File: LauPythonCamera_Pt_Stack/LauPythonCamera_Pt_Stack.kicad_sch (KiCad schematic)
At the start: 42 parts, among them J1 DF40C-80DP (Bank A), J2 DF40C-80DP (Bank B), J3 DF40C-50DP (Control), U1 NOIP1SN1300A-QDI, U2 AP2112K-1.8 LDO, U3 Load switch 3V3, U4 ADP7158-3.3

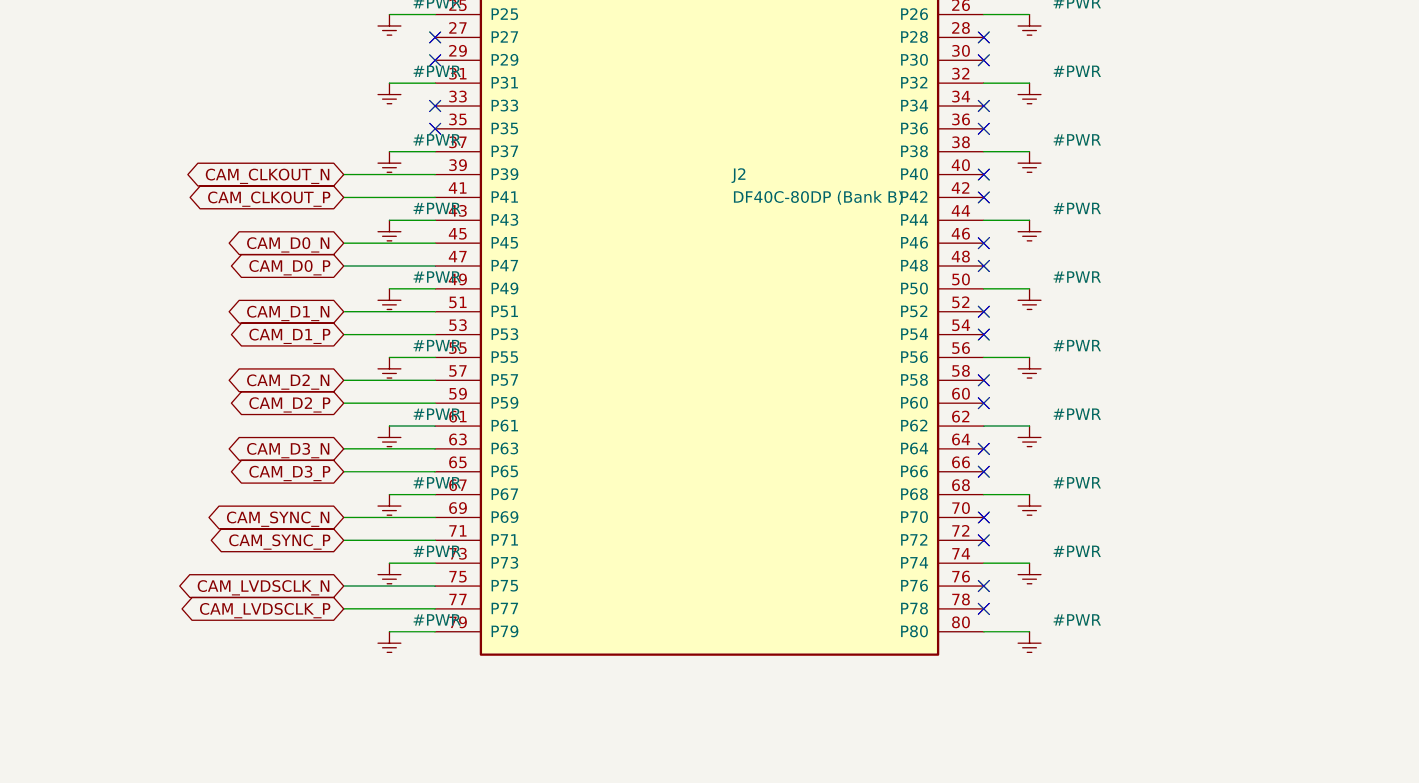
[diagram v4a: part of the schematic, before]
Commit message: fix(camera): MIRRORED FOOTPRINT + LVDS moves to the DF40's even row
Two serious bugs, both surfaced by the reminder that the DF40s are on the BOTTOM
and the sensor is on the TOP. Both would have scrapped a board.

===========================================================================
BUG 1 — THE FOOTPRINT WAS MIRRORED
===========================================================================

KiCad's canvas has +y DOWN. The datasheet drawings use +y UP. The footprint was
built straight from the datasheet without converting.

Result: numbering ran CLOCKWISE on the canvas where the real part runs
COUNTER-CLOCKWISE. No rotation of a physical part can fix a mirrored footprint.

    shipped   : left edge, top->bottom = 6, 5, 4, 3, 2, 1, 48, 47, 46, 45, 44, 43
    corrected : left edge, top->bottom = 43, 44, 45, 46, 47, 48, 1, 2, 3, 4, 5, 6
    datasheet : Fig 51 reads 45, 48, 1, 5 going DOWN -> numbers INCREASE downward

It passed every other check — 48 pads, correct pitch, pins 7-18 contiguous,
correct index holes — because none of them looked at HANDEDNESS. The generator
even carried a CONFIRMED=False guard built specifically against this class of
error; the guard verified the datasheet READING and then the implementation used
the wrong coordinate system anyway.

There is now a chirality assert, and it FIRES on the old map. That one line is
the whole test. If the footprint is ever regenerated, keep it.

===========================================================================
BUG 2 — LVDS WAS ON THE WRONG DF40 ROW
===========================================================================

The DF40's two rows escape in OPPOSITE directions (odd at y=+1.355, even at
y=-1.355; tails splay outward). On the real element board — measured from the
FABBED LauCameraTrigger_Alchitry_Stack — Bank B sits at y=41 on a 55x45 mm board.
So its ODD row escapes into a 2.6 mm strip against the board edge.

A 16.76 mm socket cannot fit below Bank B. The sensor MUST sit above it. T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
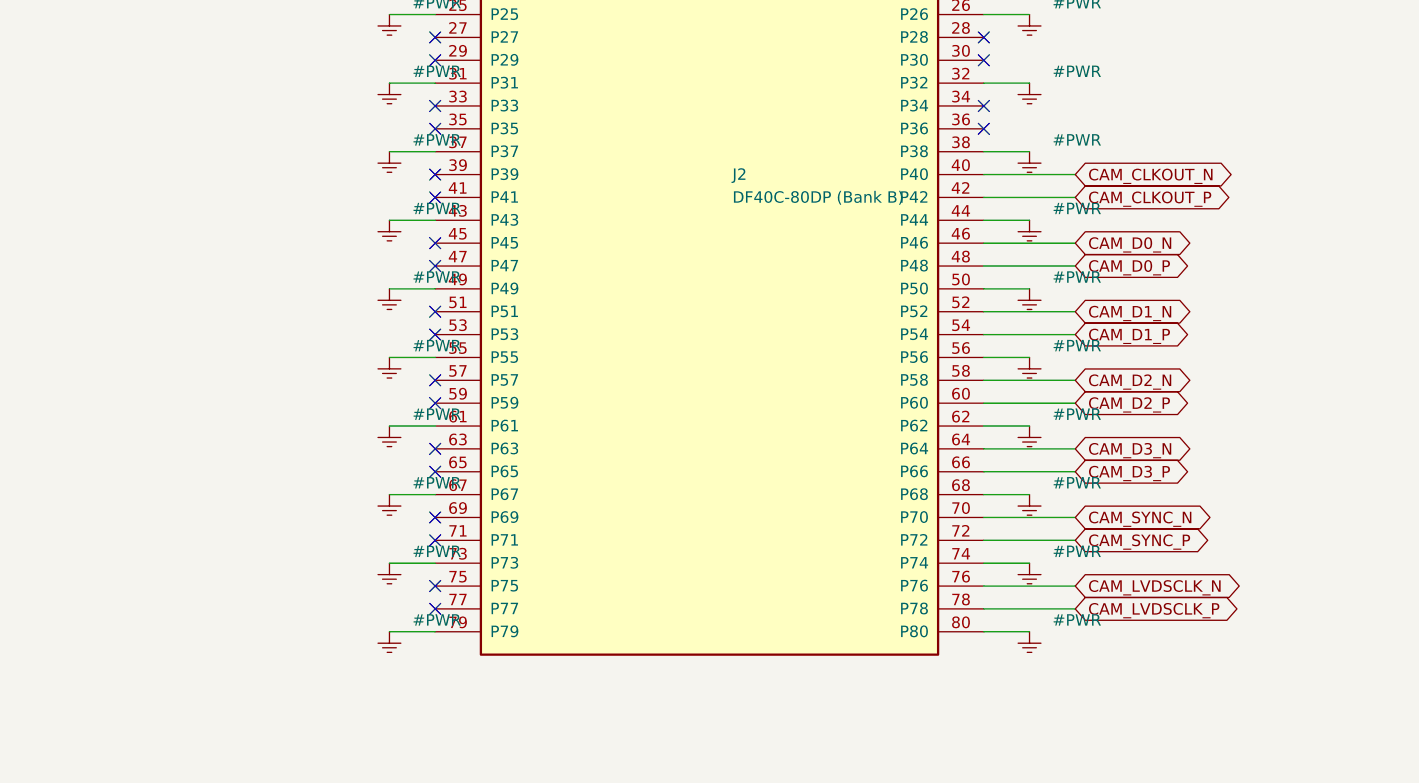
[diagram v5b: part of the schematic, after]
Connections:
- net CAM_CLKOUT_N: now also J2.40 (P40); no longer J2.39 (P39)
- net CAM_CLKOUT_P: now also J2.42 (P42); no longer J2.41 (P41)
- net CAM_D0_N: now also J2.46 (P46); no longer J2.45 (P45)
- net CAM_D0_P: now also J2.48 (P48); no longer J2.47 (P47)
- net CAM_D1_N: now also J2.52 (P52); no longer J2.51 (P51)
- net CAM_D1_P: now also J2.54 (P54); no longer J2.53 (P53)
- net CAM_D2_N: now also J2.58 (P58); no longer J2.57 (P57)
- net CAM_D2_P: now also J2.60 (P60); no longer J2.59 (P59)
- net CAM_D3_N: now also J2.64 (P64); no longer J2.63 (P63)
- net CAM_D3_P: now also J2.66 (P66); no longer J2.65 (P65)
- net CAM_LVDSCLK_N: now also J2.76 (P76); no longer J2.75 (P75)
- net CAM_LVDSCLK_P: now also J2.78 (P78); no longer J2.77 (P77)
- net CAM_SYNC_N: now also J2.70 (P70); no longer J2.69 (P69)
- net CAM_SYNC_P: now also J2.72 (P72); no longer J2.71 (P71)

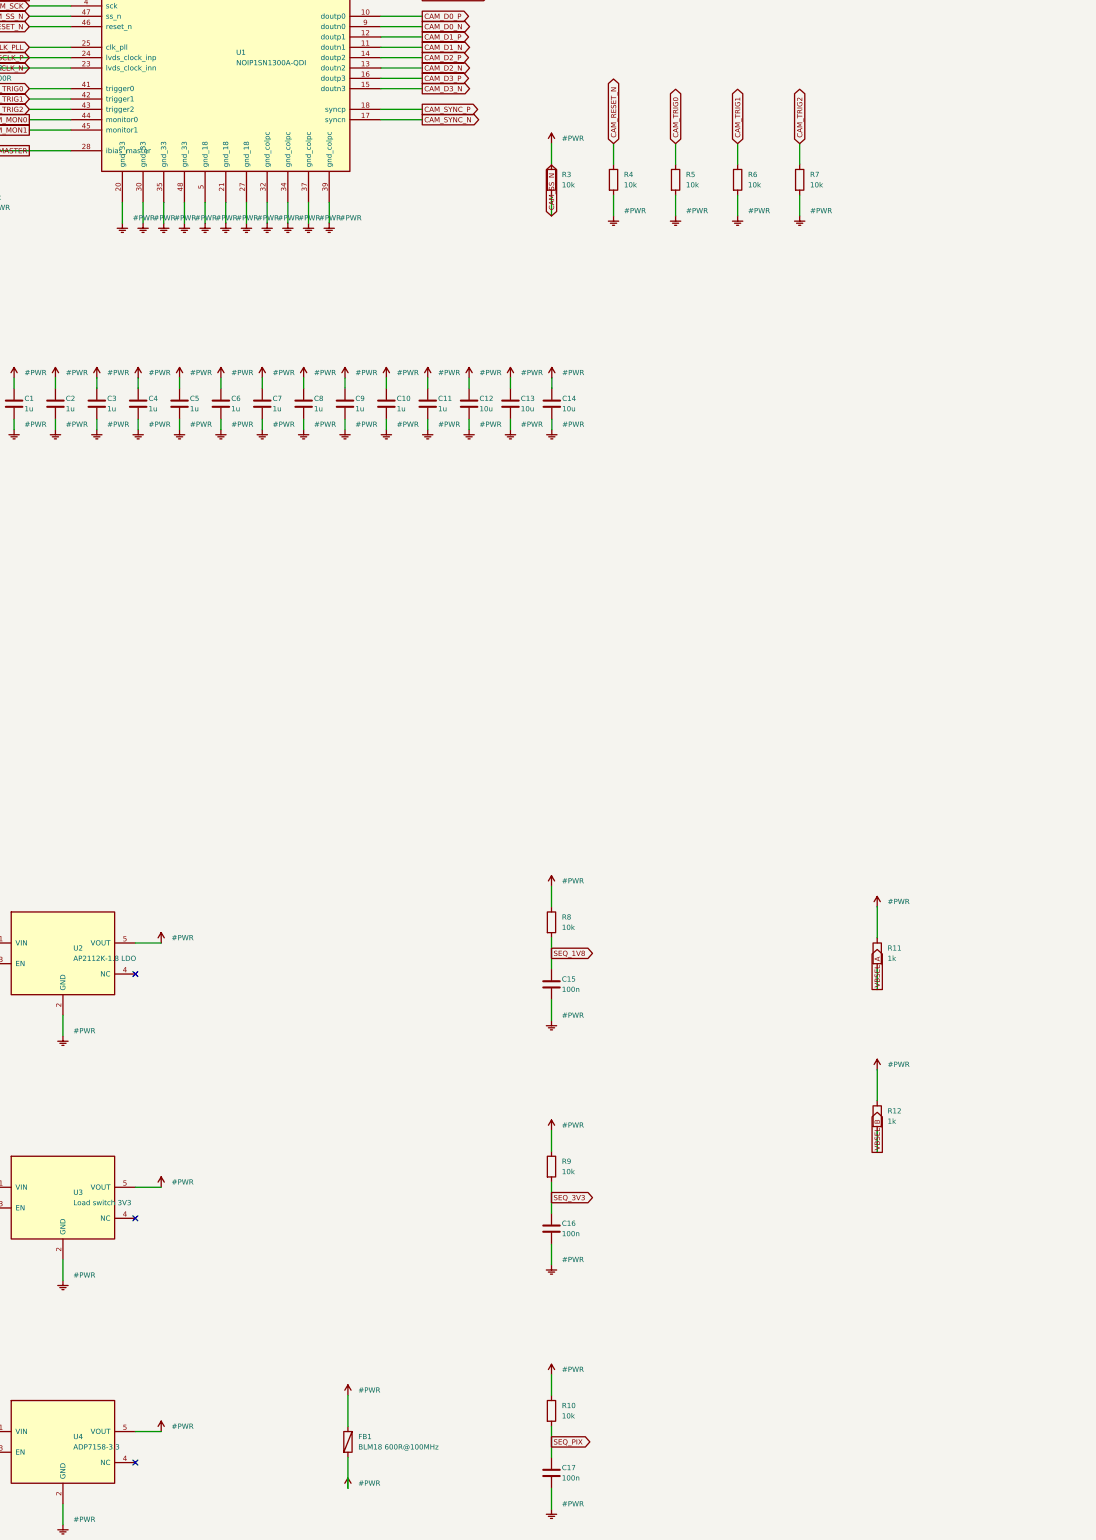
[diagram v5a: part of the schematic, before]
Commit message: fix(camera): schematic audit — D2 (LDO cap behind the bead), D4, D5, D6
Adversarial audit of the schematic against the datasheet. Six defects. Four fixed
here; D1 and D3 need design decisions and follow.

D2 — U4's LDO OUTPUT CAP WAS BEHIND THE FERRITE. (serious)
     +3V3_PIX_RAW had ZERO capacitance. Every vdd_pix cap sat behind FB1.
     An LDO's output capacitor is part of its COMPENSATION LOOP and must be at the
     VOUT pin. With a bead in series, the bead's impedance swamps the cap's at the
     loop crossover, the output pole moves, and the regulator can peak or
     oscillate — on the one rail whose entire purpose is to be quiet.
     This was introduced when FB1 was added (the ferrite was correct; its
     placement relative to the caps was not).
     FIX: C23 (2u2) directly on U4.VOUT, on the RAW side of the bead.

D4 — U3's Rds(on) WAS UNSPECIFIED. (moderate)
     vdd_33 is UNREGULATED — +3V3_SYS through a pass FET — against a +/-3% window
     (3.2-3.4 V) at 140 mA. A typical cheap SOT-23-5 switch at 500 mOhm drops
     70 mV and lands vdd_33 at 3.16 V, UNDER the 3.2 V minimum.
     FIX: specified Rds(on) <= 100 mOhm. Same class of trap as U4's +/-1%.

D5 — THREE SENSOR CMOS INPUTS FLOATED THROUGH FPGA CONFIG. (moderate)
     mosi, sck and clk_pll had no pull. FPGA user I/O are Hi-Z until DONE, so all
     three float at an indeterminate level for the whole config window with vdd_33
     already up -> crowbar current in the sensor's input buffers.
     I had exempted them because mosi/sck are "inert while ss_n is deasserted".
     THAT IS A LOGIC ARGUMENT, NOT AN ELECTRICAL ONE. They are CMOS input buffers
     regardless of what the protocol is doing.
     FIX: R13/R14/R15, 10k pull-downs. Every sensor CMOS input now has a pull —
     all eight of them.

D6 — README CONTRADICTED ITSELF. (moderate, but the kind that scraps a board)
     Section 6.6 still said the LVDS pairs were "all on the ODD row" — the exact
     error section 5.1.1 was written to p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
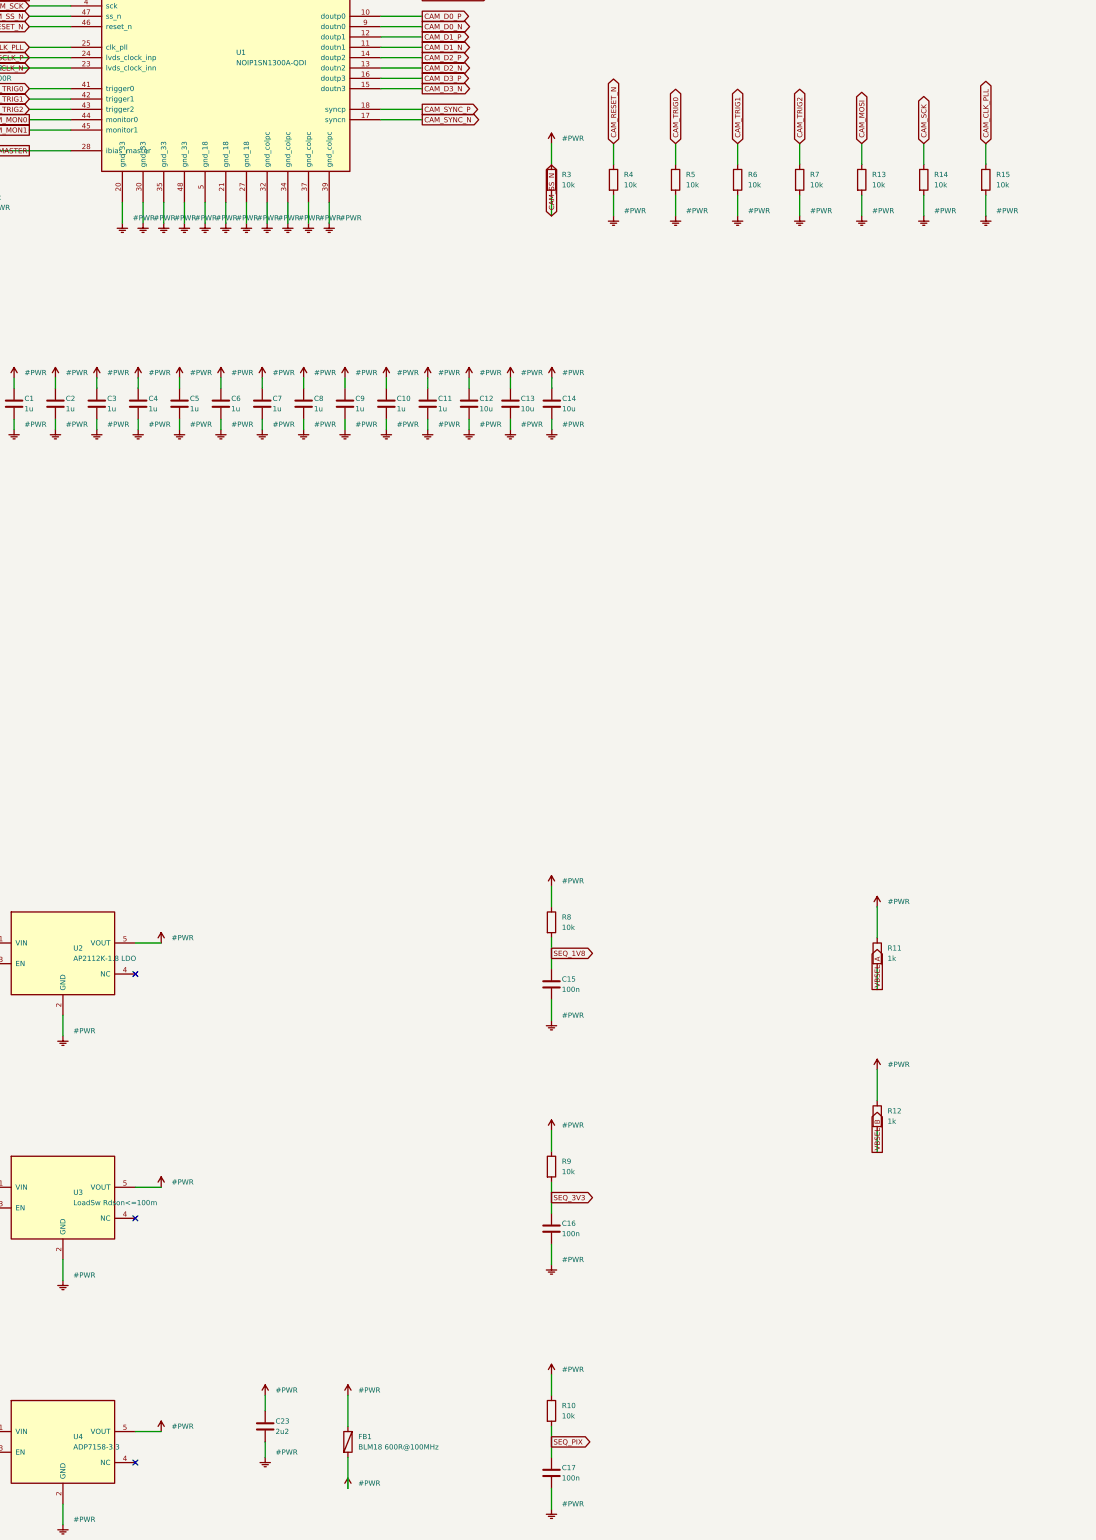
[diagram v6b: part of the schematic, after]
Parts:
- added C23: 2u2, Capacitor_SMD:C_0402_1005Metric, symbol Device:C
- added R13, R14, R15: 10k, Resistor_SMD:R_0402_1005Metric, symbol Device:R
- U3: value Load switch 3V3 -> LoadSw Rdson<=100m
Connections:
- net +3V3_PIX_RAW: now also C23.1
- net CAM_CLK_PLL: now also R15.1
- net CAM_MOSI: now also R13.1
- net CAM_SCK: now also R14.1
- net GND: now also C23.2, R13.2, R14.2, R15.2
